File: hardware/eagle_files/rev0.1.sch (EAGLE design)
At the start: 11 parts, among them U1 AD8332ACPZ-R7, U2 AD8333ACPZ-REEL, U3 AD8021ARMZ, U4 AD8021ARMZ

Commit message: Completed Preamplifier stage of the design
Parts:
- added C1, C42: 0.1uF, resistor:C-USC1206
- added C2: 22pF, resistor:C-USC1206
- added C39: 0.018uF, resistor:C-USC1206
- added C43: 1nF, resistor:C-USC1206
- added L1, L5: 120nH, resistor:R-US_R0603
- added R1: 0, resistor:R-US_R1206
- added R9: 274, resistor:R-US_R0603
- added SMA_IN_1: 901-143, Amphenol_By_element14_Batch_1:901-143
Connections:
- new net +5V: L5.2
- new net INH1: C1.2, C2.1, C39.2, U1.INH1
- new net N$4: C1.1, L1.2
- new net N$6: C39.1, R9.1
- new net N$7: L1.1, SMA_IN_1.1
- new net VPSV: C42.1, C43.1, L5.1, R1.1, U1.VPSV
- net GND: now also C2.2, C42.2, C43.2
- net LON1: now also R9.2
- net VPS: now also R1.2
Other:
- note added: "AD8332"
- note added: "RF Input"
- note added: "VPSV"
- moved on the sheet: U2, U3, U4
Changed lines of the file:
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@@
 <part name="C13" library="resistor" deviceset="C-US" device="C1206" value="0.1uF"/>
 <part name="GND6" library="supply1" deviceset="GND" device=""/>
+<part name="L1" library="resistor" deviceset="R-US_" device="R0603" value="120nH"/>
+<part name="C1" library="resistor" deviceset="C-US" device="C1206" value="0.1uF"/>
+<part name="C2" library="resistor" deviceset="C-US" device="C1206" value="22pF"/>
+<part name="C39" library="resistor" deviceset="C-US" device="C1206" value="0.018uF"/>
+<part name="R9" library="resistor" deviceset="R-US_" device="R0603" value="274"/>
+<part name="SMA_IN_1" library="Amphenol_By_element14_Batch_1" deviceset="901-143" device=""/>
+<part name="GND7" library="supply1" deviceset="GND" device=""/>
+<part name="L5" library="resistor" deviceset="R-US_" device="R0603" value="120nH"/>
+<part name="C42" library="resistor" deviceset="C-US" device="C1206" value="0.1uF"/>
+<part name="C43" library="resistor" deviceset="C-US" device="C1206" value="1nF"/>
+<part name="GND8" library="supply1" deviceset="GND" device=""/>
+<part name="GND9" library="supply1" deviceset="GND" device=""/>
+<part name="SUPPLY1" library="supply2" deviceset="+5V" device=""/>
+<part name="R1" library="resistor" deviceset="R-US_" device="R1206" value="0"/>
 </parts>
 <sheets>
@@
 <text x="5.08" y="53.34" size="0.8128" layer="91">Intentionally Blank</text>
 <text x="27.94" y="86.36" size="0.8128" layer="91">Intentionally Blank</text>
+<frame x1="-167.64" y1="15.24" x2="-60.96" y2="91.44" columns="8" rows="5" layer="91"/>
+<text x="-96.52" y="22.86" size="5.08" layer="91">RF Input</text>
+<frame x1="-147.32" y1="109.22" x2="-83.82" y2="172.72" columns="8" rows="5" layer="91"/>
+<text x="-106.68" y="114.3" size="5.08" layer="91">VPSV</text>
+<frame x1="-40.64" y1="-15.24" x2="88.9" y2="109.22" columns="8" rows="5" layer="91"/>
+<text x="58.42" y="-10.16" size="5.08" layer="91">AD8332</text>
 </plain>
 <instances>
@@
 <attribute name="VALUE" x="10.16" y="76.2" size="2.54" layer="96" ratio="10" rot="SR0"/>
 </instance>
-<instance part="U2" gate="A" x="116.84" y="73.66"/>
-<instance part="U3" gate="A" x="215.9" y="78.74"/>
-<instance part="U4" gate="A" x="218.44" y="25.4"/>
+<instance part="U2" gate="A" x="175.26" y="63.5"/>
+<instance part="U3" gate="A" x="274.32" y="68.58"/>
+<instance part="U4" gate="A" x="276.86" y="15.24"/>
 <instance part="C6" gate="G$1" x="58.42" y="63.5"/>
 <instance part="C5" gate="G$1" x="66.04" y="63.5"/>
@@
 </instance>
 <instance part="GND6" gate="1" x="-20.32" y="68.58"/>
+<instance part="L1" gate="G$1" x="-111.76" y="45.72" smashed="yes" rot="R90">
+<attribute name="NAME" x="-105.41" y="46.7614" size="1.778" layer="95" rot="R180"/>
+<attribute name="VALUE" x="-102.87" y="43.942" size="1.778" layer="96" rot="R180"/>
+</instance>
+<instance part="C1" gate="G$1" x="-104.14" y="53.34" smashed="yes" rot="R90">
+<attribute name="NAME" x="-105.156" y="57.785" size="1.778" layer="95" rot="R180"/>
+<attribute name="VALUE" x="-105.156" y="54.991" size="1.778" layer="96" rot="R180"/>
+</instance>
+<instance part="C2" gate="G$1" x="-91.44" y="48.26"/>
+<instance part="C39" gate="G$1" x="-91.44" y="60.96"/>
+<instance part="R9" gate="G$1" x="-91.44" y="71.12" smashed="yes" rot="R90">
+<attribute name="NAME" x="-85.09" y="72.1614" size="1.778" layer="95" rot="R180"/>
+<attribute name="VALUE" x="-85.09" y="69.342" size="1.778" layer="96" rot="R180"/>
+</instance>
+<instance part="SMA_IN_1" gate="A" x="-127" y="35.56" smashed="yes" rot="R180">
+<attribute name="NAME" x="-127.3556" y="41.6814" size="2.0828" layer="95" ratio="10" rot="SR180"/>
+<attribute name="VALUE" x="-129.6924" y="37.465" size="2.0828" layer="96" ratio="10" rot="SR180"/>
+</instance>
+<instance part="GND7" gate="1" x="-91.44" y="40.64"/>
+<instance part="L5" gate="G$1" x="-109.22" y="149.86" smashed="yes" rot="R90">
+<attribute name="NAME" x="-102.87" y="150.9014" size="1.778" layer="95" rot="R180"/>
+<attribute name="VALUE" x="-100.33" y="148.082" size="1.778" layer="96" rot="R180"/>
+</instance>
+<instance part="C42" gate="G$1" x="-119.38" y="137.16"/>
+<instance part="C43" gate="G$1" x="-109.22" y="137.16"/>
+<instance part="GND8" gate="1" x="-109.22" y="129.54"/>
+<instance part="GND9" gate="1" x="-119.38" y="129.54"/>
+<instance part="SUPPLY1" gate="+5V" x="-109.22" y="157.48"/>
+<instance part="R1" gate="G$1" x="-121.92" y="149.86" smashed="yes" rot="R90">
+<attribute name="NAME" x="-115.57" y="150.9014" size="1.778" layer="95" rot="R180"/>
+<attribute name="VALUE" x="-115.57" y="148.082" size="1.778" layer="96" rot="R180"/>
+</instance>
 </instances>
 <busses>
@@
 <label x="-15.24" y="73.66" size="1.778" layer="95"/>
 </segment>
+<segment>
+<pinref part="C2" gate="G$1" pin="2"/>
+<pinref part="GND7" gate="1" pin="GND"/>
+</segment>
+<segment>
+<pinref part="C43" gate="G$1" pin="2"/>
+<pinref part="GND8" gate="1" pin="GND"/>
+</segment>
+<segment>
+<pinref part="C42" gate="G$1" pin="2"/>
+<pinref part="GND9" gate="1" pin="GND"/>
+</segment>
 </net>
 <net name="LMD1" class="0">
@@
 </segment>
 </net>
-<net name="LON1" class="0">
-<segment>
-<pinref part="U1" gate="A" pin="LON1"/>
-<pinref part="R26" gate="G$1" pin="1"/>
-<wire x1="50.8" y1="45.72" x2="53.34" y2="45.72" width="0.1524" layer="91"/>
-</segment>
-</net>
 <net name="LOP1" class="0">
 <segment>
@@
 <segment>
 <pinref part="U2" gate="A" pin="RF1P"/>
-<wire x1="116.84" y1="48.26" x2="114.3" y2="48.26" width="0.1524" layer="91"/>
-<label x="109.22" y="48.26" size="1.778" layer="95"/>
+<wire x1="175.26" y1="38.1" x2="172.72" y2="38.1" width="0.1524" layer="91"/>
+<label x="167.64" y="38.1" size="1.778" layer="95"/>
 </segment>
 </net>
@@
 <segment>
 <pinref part="U2" gate="A" pin="RF1N"/>
-<wire x1="116.84" y1="50.8" x2="114.3" y2="50.8" width="0.1524" layer="91"/>
-<label x="109.22" y="50.8" size="1.778" layer="95"/>
+<wire x1="175.26" y1="40.64" x2="172.72" y2="40.64" width="0.1524" layer="91"/>
+<label x="167.64" y="40.64" size="1.778" layer="95"/>
 </segment>
 </net>
@@
 <label x="-15.24" y="10.16" size="1.778" layer="95"/>
 </segment>
+<segment>
+<pinref part="R1" gate="G$1" pin="2"/>
+<wire x1="-121.92" y1="154.94" x2="-121.92" y2="157.48" width="0.1524" layer="91"/>
+<label x="-121.92" y="160.02" size="1.778" layer="95" rot="R180"/>
+</segment>
 </net>
 <net name="N$3" class="0">
@@
 </segment>
 </net>
+<net name="INH1" class="0">
+<segment>
+<pinref part="C1" gate="G$1" pin="2"/>
+<pinref part="C2" gate="G$1" pin="1"/>
+<wire x1="-99.06" y1="53.34" x2="-91.44" y2="53.34" width="0.1524" layer="91"/>
+<pinref part="C39" gate="G$1" pin="2"/>
+<wire x1="-91.44" y1="50.8" x2="-91.44" y2="53.34" width="0.1524" layer="91"/>
+<junction x="-91.44" y="53.34"/>
+<wire x1="-91.44" y1="53.34" x2="-91.44" y2="55.88" width="0.1524" layer="91"/>
+<wire x1="-91.44" y1="53.34" x2="-88.9" y2="53.34" width="0.1524" layer="91"/>
+<label x="-88.9" y="53.34" size="1.778" layer="95"/>
+</segment>
+<segment>
+<pinref part="U1" gate="A" pin="INH1"/>
+<wire x1="-10.16" y1="68.58" x2="-12.7" y2="68.58" width="0.1524" layer="91"/>
+<label x="-15.24" y="68.58" size="1.778" layer="95"/>
+</segment>
+</net>
+<net name="N$6" class="0">
+<segment>
+<pinref part="C39" gate="G$1" pin="1"/>
+<pinref part="R9" gate="G$1" pin="1"/>
+<wire x1="-91.44" y1="63.5" x2="-91.44" y2="66.04" width="0.1524" layer="91"/>
+</segment>
+</net>
+<net name="N$4" class="0">
+<segment>
+<pinref part="C1" gate="G$1" pin="1"/>
+<pinref part="L1" gate="G$1" pin="2"/>
+<wire x1="-106.68" y1="53.34" x2="-111.76" y2="53.34" width="0.1524" layer="91"/>
+<wire x1="-111.76" y1="53.34" x2="-111.76" y2="50.8" width="0.1524" layer="91"/>
+</segment>
+</net>
+<net name="N$7" class="0">
+<segment>
+<pinref part="SMA_IN_1" gate="A" pin="1"/>
+<pinref part="L1" gate="G$1" pin="1"/>
+<wire x1="-114.3" y1="38.1" x2="-111.76" y2="38.1" width="0.1524" layer="91"/>
+<wire x1="-111.76" y1="38.1" x2="-111.76" y2="40.64" width="0.1524" layer="91"/>
+</segment>
+</net>
+<net name="LON1" class="0">
+<segment>
+<pinref part="U1" gate="A" pin="LON1"/>
+<pinref part="R26" gate="G$1" pin="1"/>
+<wire x1="50.8" y1="45.72" x2="53.34" y2="45.72" width="0.1524" layer="91"/>
+</segment>
+<segment>
+<pinref part="R9" gate="G$1" pin="2"/>
+<wire x1="-91.44" y1="76.2" x2="-91.44" y2="78.74" width="0.1524" layer="91"/>
+<label x="-93.98" y="78.74" size="1.778" layer="95"/>
+</segment>
+</net>
+<net name="VPSV" class="0">
+<segment>
+<pinref part="L5" gate="G$1" pin="1"/>
+<wire x1="-109.22" y1="144.78" x2="-109.22" y2="142.24" width="0.1524" layer="91"/>
+<wire x1="-109.22" y1="142.24" x2="-119.38" y2="142.24" width="0.1524" layer="91"/>
+<pinref part="C42" gate="G$1" pin="1"/>
+<wire x1="-119.38" y1="142.24" x2="-119.38" y2="139.7" width="0.1524" layer="91"/>
+<pinref part="C43" gate="G$1" pin="1"/>
+<wire x1="-109.22" y1="142.24" x2="-109.22" y2="139.7" width="0.1524" layer="91"/>
+<wire x1="-119.38" y1="142.24" x2="-121.92" y2="142.24" width="0.1524" layer="91"/>
+<label x="-132.08" y="142.24" size="1.778" layer="95"/>
+<wire x1="-121.92" y1="142.24" x2="-127" y2="142.24" width="0.1524" layer="91"/>
+<wire x1="-121.92" y1="142.24" x2="-121.92" y2="144.78" width="0.1524" layer="91"/>
+<junction x="-121.92" y="142.24"/>
+<pinref part="R1" gate="G$1" pin="1"/>
+</segment>
+<segment>
+<pinref part="U1" gate="A" pin="VPSV"/>
+<wire x1="-10.16" y1="17.78" x2="-12.7" y2="17.78" width="0.1524" layer="91"/>
+<label x="-15.24" y="17.78" size="1.778" layer="95"/>
+</segment>
+</net>
+<net name="+5V" class="0">
+<segment>
+<pinref part="L5" gate="G$1" pin="2"/>
+<pinref part="SUPPLY1" gate="+5V" pin="+5V"/>
+</segment>
+</net>

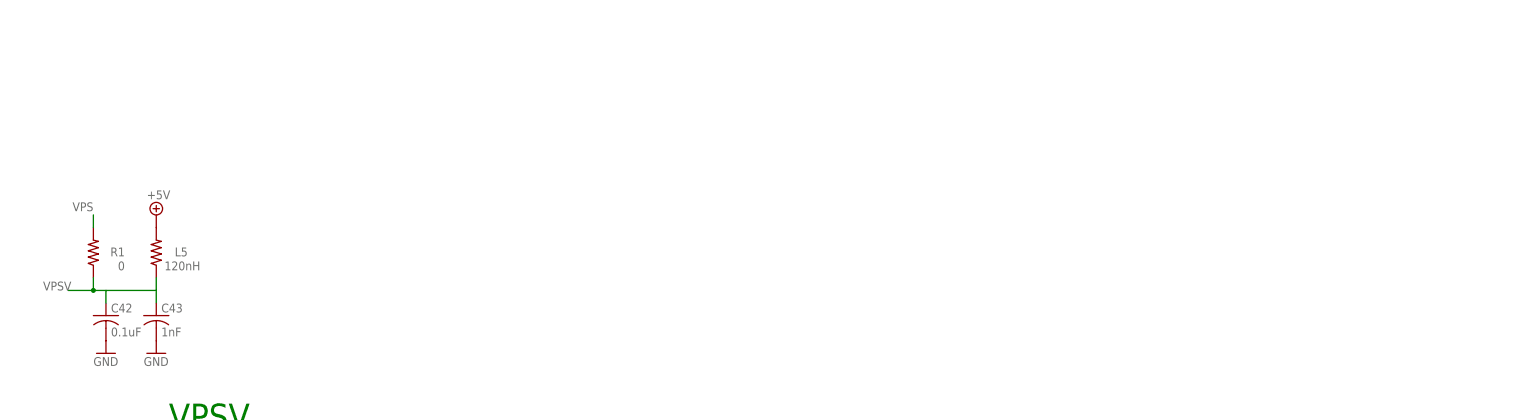
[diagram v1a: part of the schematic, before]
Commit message: Added Local Osc
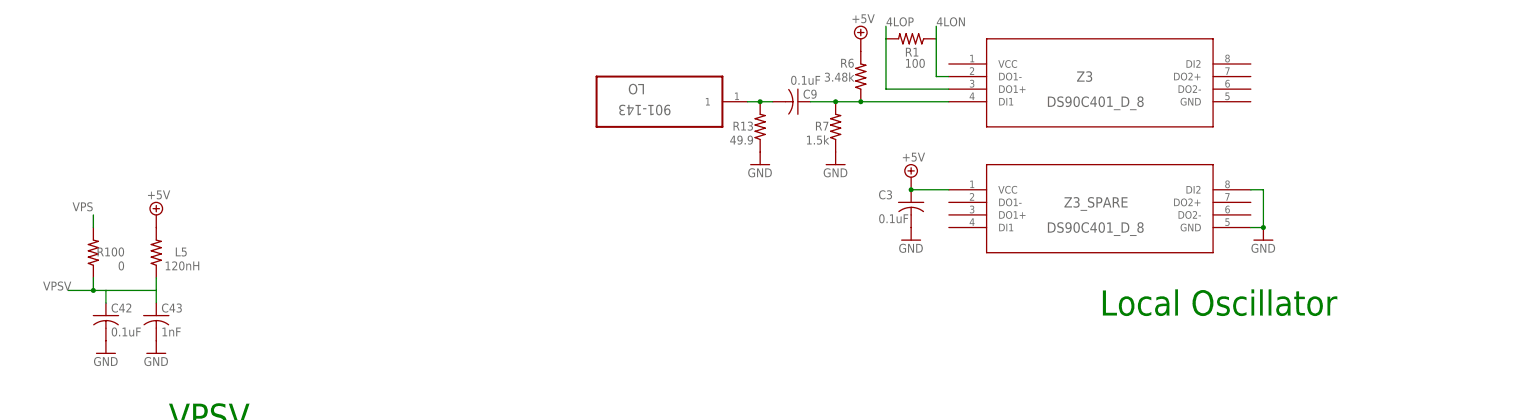
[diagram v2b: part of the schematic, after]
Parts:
- added C3, C9: 0.1uF, resistor:C-USC1206
- added LO: 901-143, Amphenol_By_element14_Batch_1:901-143
- added R100: 0, resistor:R-US_R1206
- added R13: 49.9, resistor:R-US_R1206
- added R6: 3.48k, resistor:R-US_R1206
- added R7: 1.5k, resistor:R-US_R1206
- added Z3, Z3_SPARE: DS90C401_D_8, ds90c401:DS90C401_D_8
- R1: value 0 -> 100
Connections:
- new net 4LON: R1.1, Z3.DO1-
- new net 4LOP: R1.2, Z3.DO1+
- new net N$5: C9.1, R6.1, R7.2, Z3.DI1
- new net N$8: C9.2, LO.1, R13.2
- net +5V: now also C3.1, R6.2, Z3_SPARE.VCC
- net GND: now also C3.2, R13.1, R7.1, Z3_SPARE.DI2, Z3_SPARE.GND
- net VPS: now also R100.2; no longer R1.2
- net VPSV: now also R100.1; no longer R1.1
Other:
- note added: "Local Oscillator"
- moved on the sheet: R1
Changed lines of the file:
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@@
 <part name="GND9" library="supply1" deviceset="GND" device=""/>
 <part name="SUPPLY1" library="supply2" deviceset="+5V" device=""/>
-<part name="R1" library="resistor" deviceset="R-US_" device="R1206" value="0"/>
+<part name="R100" library="resistor" deviceset="R-US_" device="R1206" value="0"/>
+<part name="Z3" library="ds90c401" deviceset="DS90C401_D_8" device=""/>
+<part name="Z3_SPARE" library="ds90c401" deviceset="DS90C401_D_8" device=""/>
+<part name="C3" library="resistor" deviceset="C-US" device="C1206" value="0.1uF"/>
+<part name="C9" library="resistor" deviceset="C-US" device="C1206" value="0.1uF"/>
+<part name="GND10" library="supply1" deviceset="GND" device=""/>
+<part name="SUPPLY2" library="supply2" deviceset="+5V" device=""/>
+<part name="GND11" library="supply1" deviceset="GND" device=""/>
+<part name="SUPPLY3" library="supply2" deviceset="+5V" device=""/>
+<part name="R6" library="resistor" deviceset="R-US_" device="R1206" value="3.48k"/>
+<part name="LO" library="Amphenol_By_element14_Batch_1" deviceset="901-143" device=""/>
+<part name="R7" library="resistor" deviceset="R-US_" device="R1206" value="1.5k"/>
+<part name="GND12" library="supply1" deviceset="GND" device=""/>
+<part name="R13" library="resistor" deviceset="R-US_" device="R1206" value="49.9"/>
+<part name="GND13" library="supply1" deviceset="GND" device=""/>
+<part name="R1" library="resistor" deviceset="R-US_" device="R1206" value="100"/>
 </parts>
 <sheets>
@@
 <frame x1="-40.64" y1="-15.24" x2="88.9" y2="109.22" columns="8" rows="5" layer="91"/>
 <text x="58.42" y="-10.16" size="5.08" layer="91">AD8332</text>
+<frame x1="-35.56" y1="129.54" x2="134.62" y2="213.36" columns="8" rows="5" layer="91"/>
+<text x="81.28" y="137.16" size="5.08" layer="91">Local Oscillator</text>
 </plain>
 <instances>
@@
 <instance part="GND9" gate="1" x="-119.38" y="129.54"/>
 <instance part="SUPPLY1" gate="+5V" x="-109.22" y="157.48"/>
-<instance part="R1" gate="G$1" x="-121.92" y="149.86" smashed="yes" rot="R90">
+<instance part="R100" gate="G$1" x="-121.92" y="149.86" smashed="yes" rot="R90">
 <attribute name="NAME" x="-115.57" y="150.9014" size="1.778" layer="95" rot="R180"/>
 <attribute name="VALUE" x="-115.57" y="148.082" size="1.778" layer="96" rot="R180"/>
+</instance>
+<instance part="Z3" gate="A" x="50.8" y="187.96" smashed="yes">
+<attribute name="NAME" x="76.5556" y="184.3786" size="2.0828" layer="95" ratio="6" rot="SR0"/>
+<attribute name="VALUE" x="70.5358" y="179.2986" size="2.0828" layer="96" ratio="6" rot="SR0"/>
+</instance>
+<instance part="Z3_SPARE" gate="A" x="50.8" y="162.56" smashed="yes">
+<attribute name="NAME" x="74.0156" y="158.9786" size="2.0828" layer="95" ratio="6" rot="SR0"/>
+<attribute name="VALUE" x="70.5358" y="153.8986" size="2.0828" layer="96" ratio="6" rot="SR0"/>
+</instance>
+<instance part="C3" gate="G$1" x="43.18" y="160.02" smashed="yes">
+<attribute name="NAME" x="36.576" y="160.655" size="1.778" layer="95"/>
+<attribute name="VALUE" x="36.576" y="155.829" size="1.778" layer="96"/>
+</instance>
+<instance part="C9" gate="G$1" x="20.32" y="180.34" smashed="yes" rot="R270">
+<attribute name="NAME" x="21.336" y="180.975" size="1.778" layer="95"/>
+<attribute name="VALUE" x="18.796" y="183.769" size="1.778" layer="96"/>
+</instance>
+<instance part="GND10" gate="1" x="43.18" y="152.4"/>
+<instance part="SUPPLY2" gate="+5V" x="43.18" y="165.1"/>
+<instance part="GND11" gate="1" x="114.3" y="152.4"/>
+<instance part="SUPPLY3" gate="+5V" x="33.02" y="193.04"/>
+<instance part="R6" gate="G$1" x="33.02" y="185.42" smashed="yes" rot="R90">
+<attribute name="NAME" x="31.75" y="189.0014" size="1.778" layer="95" rot="R180"/>
+<attribute name="VALUE" x="31.75" y="186.182" size="1.778" layer="96" rot="R180"/>
+</instance>
+<instance part="LO" gate="A" x="-2.54" y="177.8" smashed="yes" rot="R180">
+<attribute name="NAME" x="-10.5156" y="183.9214" size="2.0828" layer="95" ratio="10" rot="SR180"/>
+<attribute name="VALUE" x="-5.2324" y="179.705" size="2.0828" layer="96" ratio="10" rot="SR180"/>
+</instance>
+<instance part="R7" gate="G$1" x="27.94" y="175.26" smashed="yes" rot="R90">
+<attribute name="NAME" x="26.67" y="176.3014" size="1.778" layer="95" rot="R180"/>
+<attribute name="VALUE" x="26.67" y="173.482" size="1.778" layer="96" rot="R180"/>
+</instance>
+<instance part="GND12" gate="1" x="27.94" y="167.64"/>
+<instance part="R13" gate="G$1" x="12.7" y="175.26" smashed="yes" rot="R90">
+<attribute name="NAME" x="11.43" y="176.3014" size="1.778" layer="95" rot="R180"/>
+<attribute name="VALUE" x="11.43" y="173.482" size="1.778" layer="96" rot="R180"/>
+</instance>
+<instance part="GND13" gate="1" x="12.7" y="167.64"/>
+<instance part="R1" gate="G$1" x="43.18" y="193.04" smashed="yes" rot="R180">
+<attribute name="NAME" x="41.91" y="189.4586" size="1.778" layer="95"/>
+<attribute name="VALUE" x="41.91" y="187.198" size="1.778" layer="96"/>
 </instance>
 </instances>
@@
 <pinref part="GND9" gate="1" pin="GND"/>
 </segment>
+<segment>
+<pinref part="C3" gate="G$1" pin="2"/>
+<pinref part="GND10" gate="1" pin="GND"/>
+</segment>
+<segment>
+<pinref part="Z3_SPARE" gate="A" pin="DI2"/>
+<wire x1="111.76" y1="162.56" x2="114.3" y2="162.56" width="0.1524" layer="91"/>
+<wire x1="114.3" y1="162.56" x2="114.3" y2="154.94" width="0.1524" layer="91"/>
+<pinref part="Z3_SPARE" gate="A" pin="GND"/>
+<wire x1="114.3" y1="154.94" x2="111.76" y2="154.94" width="0.1524" layer="91"/>
+<pinref part="GND11" gate="1" pin="GND"/>
+<junction x="114.3" y="154.94"/>
+</segment>
+<segment>
+<pinref part="R7" gate="G$1" pin="1"/>
+<pinref part="GND12" gate="1" pin="GND"/>
+</segment>
+<segment>
+<pinref part="R13" gate="G$1" pin="1"/>
+<pinref part="GND13" gate="1" pin="GND"/>
+</segment>
 </net>
 <net name="LMD1" class="0">
@@
 </segment>
 <segment>
-<pinref part="R1" gate="G$1" pin="2"/>
+<pinref part="R100" gate="G$1" pin="2"/>
 <wire x1="-121.92" y1="154.94" x2="-121.92" y2="157.48" width="0.1524" layer="91"/>
 <label x="-121.92" y="160.02" size="1.778" layer="95" rot="R180"/>
@@
 <wire x1="-121.92" y1="142.24" x2="-121.92" y2="144.78" width="0.1524" layer="91"/>
 <junction x="-121.92" y="142.24"/>
-<pinref part="R1" gate="G$1" pin="1"/>
+<pinref part="R100" gate="G$1" pin="1"/>
 </segment>
 <segment>
@@
 <pinref part="SUPPLY1" gate="+5V" pin="+5V"/>
 </segment>
-</net>
+<segment>
+<pinref part="Z3_SPARE" gate="A" pin="VCC"/>
+<pinref part="C3" gate="G$1" pin="1"/>
+<wire x1="50.8" y1="162.56" x2="43.18" y2="162.56" width="0.1524" layer="91"/>
+<pinref part="SUPPLY2" gate="+5V" pin="+5V"/>
+<junction x="43.18" y="162.56"/>
+</segment>
+<segment>
+<pinref part="SUPPLY3" gate="+5V" pin="+5V"/>
+<pinref part="R6" gate="G$1" pin="2"/>
+</segment>
+</net>
+<net name="N$5" class="0">
+<segment>
+<pinref part="R6" gate="G$1" pin="1"/>
+<pinref part="C9" gate="G$1" pin="1"/>
+<wire x1="22.86" y1="180.34" x2="27.94" y2="180.34" width="0.1524" layer="91"/>
+<wire x1="27.94" y1="180.34" x2="33.02" y2="180.34" width="0.1524" layer="91"/>
+<pinref part="R7" gate="G$1" pin="2"/>
+<junction x="27.94" y="180.34"/>
+<pinref part="Z3" gate="A" pin="DI1"/>
+<wire x1="50.8" y1="180.34" x2="33.02" y2="180.34" width="0.1524" layer="91"/>
+<junction x="33.02" y="180.34"/>
+</segment>
+</net>
+<net name="N$8" class="0">
+<segment>
+<pinref part="C9" gate="G$1" pin="2"/>
+<pinref part="LO" gate="A" pin="1"/>
+<wire x1="10.16" y1="180.34" x2="12.7" y2="180.34" width="0.1524" layer="91"/>
+<pinref part="R13" gate="G$1" pin="2"/>
+<wire x1="12.7" y1="180.34" x2="15.24" y2="180.34" width="0.1524" layer="91"/>
+<junction x="12.7" y="180.34"/>
+</segment>
+</net>
+<net name="4LON" class="0">
+<segment>
+<pinref part="Z3" gate="A" pin="DO1-"/>
+<pinref part="R1" gate="G$1" pin="1"/>
+<wire x1="50.8" y1="185.42" x2="48.26" y2="185.42" width="0.1524" layer="91"/>
+<wire x1="48.26" y1="185.42" x2="48.26" y2="193.04" width="0.1524" layer="91"/>
+<wire x1="48.26" y1="193.04" x2="48.26" y2="195.58" width="0.1524" layer="91"/>
+<label x="48.26" y="195.58" size="1.778" layer="95"/>
+</segment>
+</net>
+<net name="4LOP" class="0">
+<segment>
+<pinref part="Z3" gate="A" pin="DO1+"/>
+<pinref part="R1" gate="G$1" pin="2"/>
+<wire x1="50.8" y1="182.88" x2="38.1" y2="182.88" width="0.1524" layer="91"/>
+<wire x1="38.1" y1="182.88" x2="38.1" y2="193.04" width="0.1524" layer="91"/>
+<wire x1="38.1" y1="193.04" x2="38.1" y2="195.58" width="0.1524" layer="91"/>
+<label x="38.1" y="195.58" size="1.778" layer="95"/>
+</segment>
+</net>
